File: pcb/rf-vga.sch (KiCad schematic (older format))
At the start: 0 parts

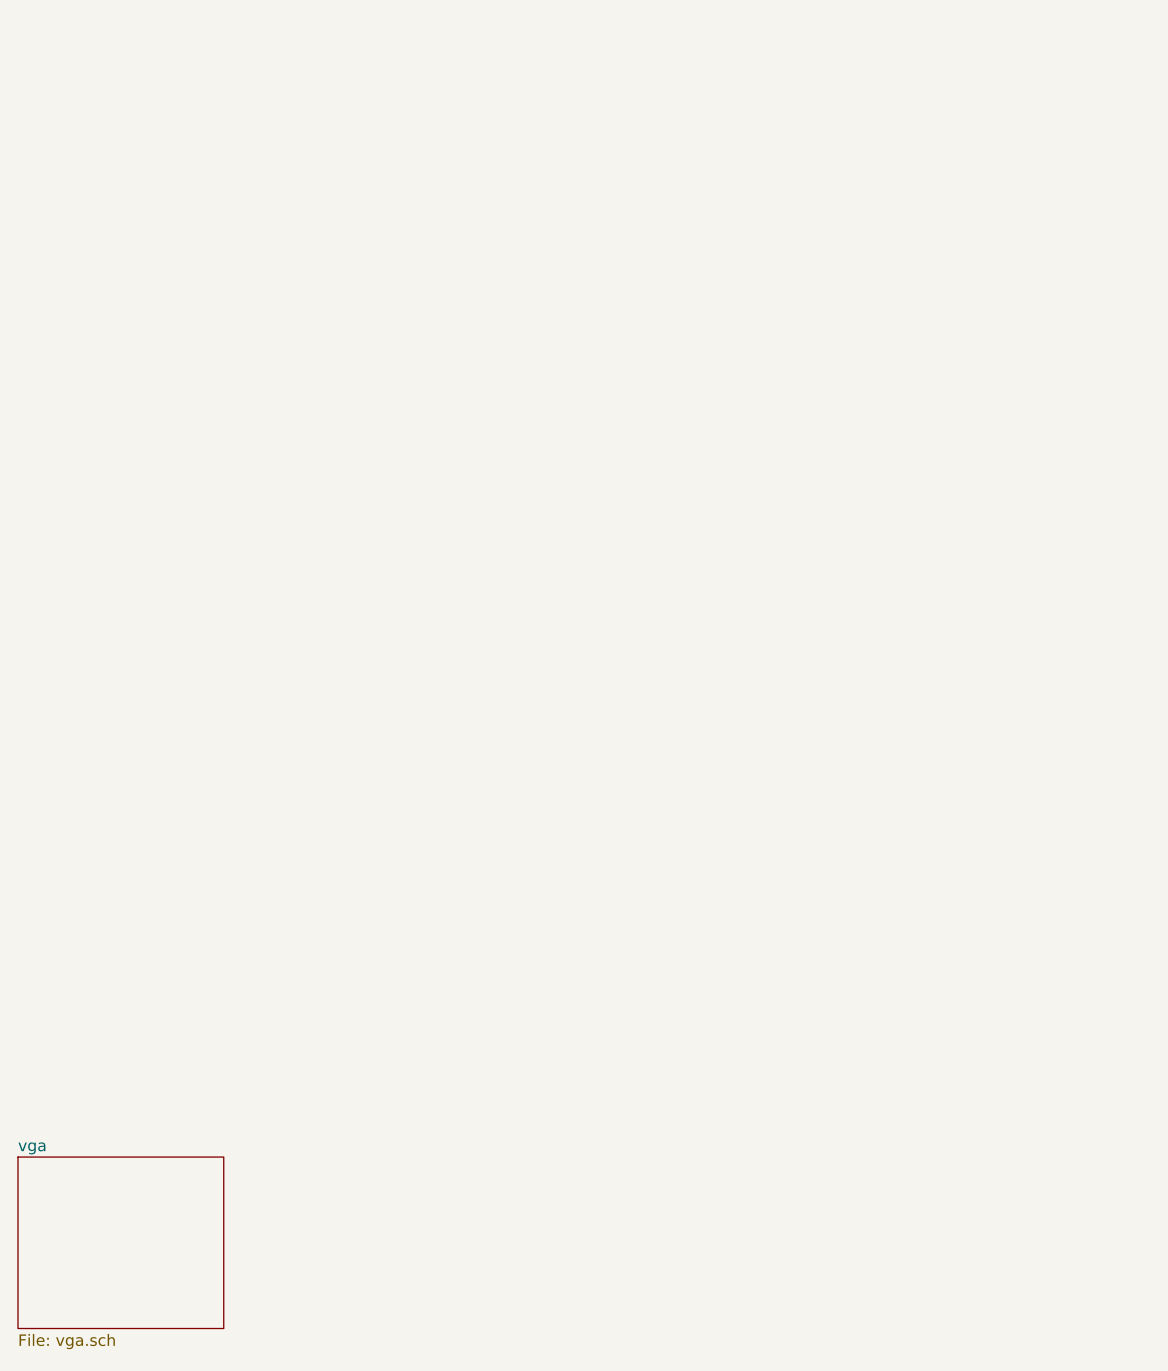
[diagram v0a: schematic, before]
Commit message: Add STM32L010C6 mcu to pcb, allocate pins
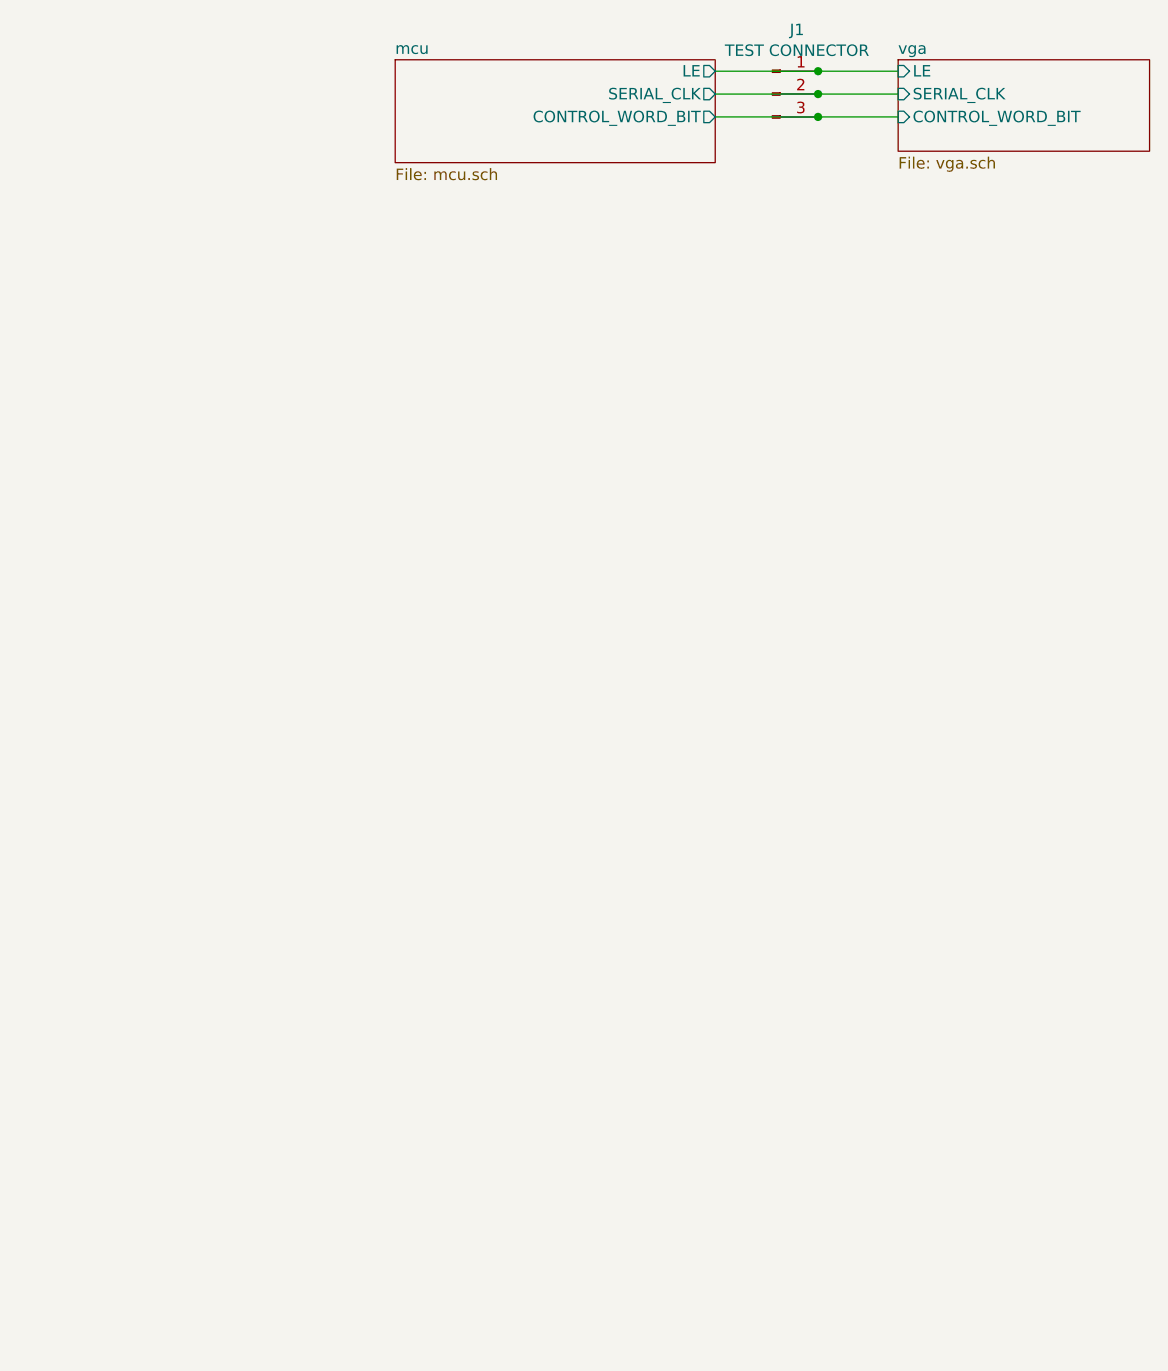
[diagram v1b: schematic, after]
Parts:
- added J1: TEST CONNECTOR, Connector_PinHeader_2.54mm:PinHeader_1x03_P2.54mm_Vertical, symbol Connector:Conn_01x03_Male
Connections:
- new net mcu/CONTROL_WORD_BIT: J1.3 (Pin_3)
- new net mcu/LE: J1.1 (Pin_1)
- new net mcu/SERIAL_CLK: J1.2 (Pin_2)
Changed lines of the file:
@@
 $Descr A4 11693 8268
 encoding utf-8
-Sheet 1 2
+Sheet 1 3
 Title ""
 Date ""
@@
 $EndDescr
 $Sheet
-S 1150 6650 900  750
+S 5000 1850 1100 400
 U 613D916B
 F0 "vga" 50
 F1 "vga.sch" 50
+F2 "LE" I L 5000 1900 50
+F3 "SERIAL_CLK" I L 5000 2000 50
+F4 "CONTROL_WORD_BIT" I L 5000 2100 50
 $EndSheet
+$Sheet
+S 2800 1850 1400 450
+U 61327CE5
+F0 "mcu" 50
+F1 "mcu.sch" 50
+F2 "LE" O R 4200 1900 50
+F3 "SERIAL_CLK" O R 4200 2000 50
+F4 "CONTROL_WORD_BIT" O R 4200 2100 50
+$EndSheet
+Wire Wire Line
+	4200 1900 4650 1900
+Wire Wire Line
+	4200 2000 4650 2000
+Wire Wire Line
+	4200 2100 4650 2100
+$Comp
+L Connector:Conn_01x03_Male J1
+U 1 1 613A2E03
+P 4450 2000
+F 0 "J1" H 4558 2281 50  0000 C CNN
+F 1 "TEST CONNECTOR" H 4558 2190 50  0000 C CNN
+F 2 "Connector_PinHeader_2.54mm:PinHeader_1x03_P2.54mm_Vertical" H 4450 2000 50  0001 C CNN
+F 3 "~" H 4450 2000 50  0001 C CNN
+	1    4450 2000
+	1    0    0    -1
+$EndComp
+Connection ~ 4650 1900
+Wire Wire Line
+	4650 1900 5000 1900
+Connection ~ 4650 2000
+Wire Wire Line
+	4650 2000 5000 2000
+Connection ~ 4650 2100
+Wire Wire Line
+	4650 2100 5000 2100
 $EndSCHEMATC

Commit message: PCB updates
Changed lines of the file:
@@
 $Descr A4 11693 8268
 encoding utf-8
-Sheet 1 3
+Sheet 1 4
 Title ""
 Date ""
@@
 Wire Wire Line
 	4650 2100 5000 2100
+$Sheet
+S 2050 3700 550  600
+U 6138BAE8
+F0 "psu" 50
+F1 "psu.sch" 50
+$EndSheet
 $EndSCHEMATC
